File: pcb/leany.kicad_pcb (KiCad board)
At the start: 4 copper layers, 86.5 x 46.5 mm, 79 parts, among them J1 ST7735S, J2 SWD, J3 USB C, J4 2059-302/998-403, Q1 AO3401A, Q2 AO3400A, Q3 AO3401A, Q4 AO3401A, SW1 SW_HIGH, SW2 SW_HIGH, SW3 SW_LOW, SW4 POWER, U1 STM32F103C8Tx, U2 CH340N, U3 ICM-42688-P, U4 BQ25619, U5 AP6683, U7 AMS1117-3.3, Y1 8MHz

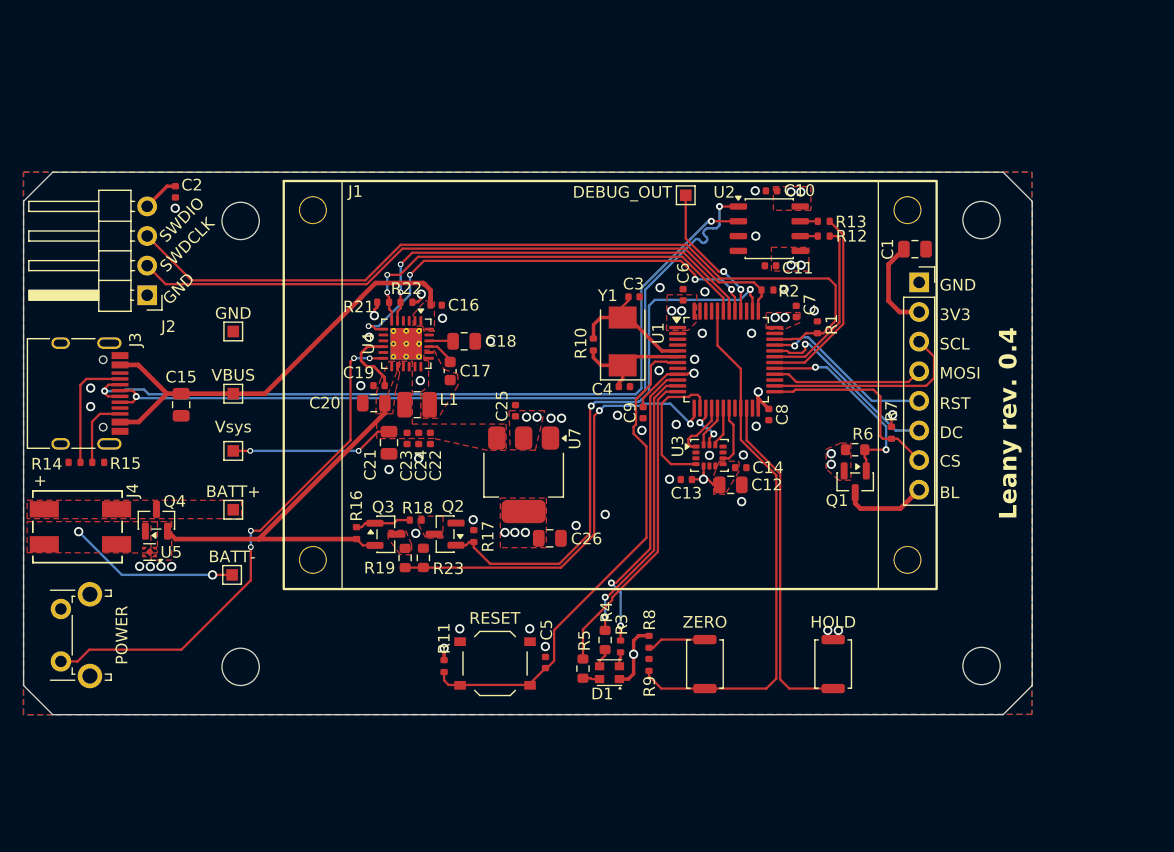
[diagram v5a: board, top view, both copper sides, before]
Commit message: refactor: fallback to rev 0.3 and update files (#98)
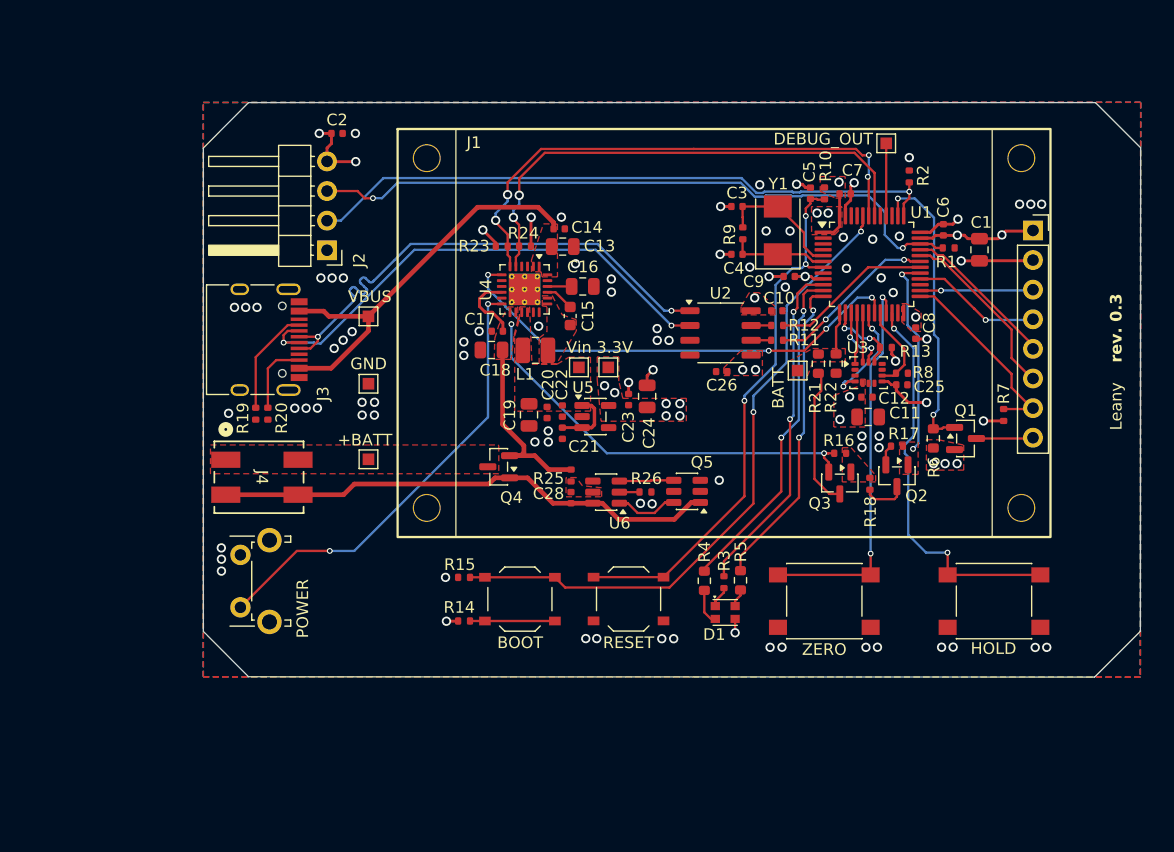
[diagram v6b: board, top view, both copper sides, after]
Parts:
- removed H1, H2, H3, H4: MountingHole, MountingHole:MountingHole_3.2mm_M3
- removed U7: AMS1117-3.3, Package_TO_SOT_SMD:SOT-223-3_TabPin2
- added C28: 100n, leany_footprints:C_0402_1005Metric, F.Cu at (136.5, 113.2)
- added Q5: PT8810, Package_TO_SOT_SMD:SOT-23-6, F.Cu at (146.5, 112.6)
- added R20: 5k1, leany_footprints:R_0402_1005Metric, F.Cu at (110.5, 106.0)
- added R24: 4k7, leany_footprints:R_0402_1005Metric, F.Cu at (132.6, 91.6)
- added R25: 100R, leany_footprints:R_0402_1005Metric, F.Cu at (136.5, 111.3)
- added R26: 1k, leany_footprints:R_0402_1005Metric, F.Cu at (142.9, 112.7)
- added SW5: POWER, Button_Switch_THT:SW_Tactile_SPST_Angled_PTS645Vx31-2LFS, F.Cu at (108.2, 122.6)
- added TP4: BATT, leany_footprints:TestPoint_Pad_1.0x1.0mm, F.Cu at (155.9, 102.3)
- added U6: DW01A, Package_TO_SOT_SMD:SOT-23-6, F.Cu at (139.5, 112.7)
- C11, C19: value 100n -> 10u; footprint leany_footprints:C_0402_1005Metric -> Capacitor_SMD:C_0805_2012Metric
- C12, C21, C26: value 10u -> 100n; footprint Capacitor_SMD:C_0805_2012Metric -> leany_footprints:C_0402_1005Metric
- C13: value 100n -> 22u; footprint leany_footprints:C_0402_1005Metric -> Capacitor_SMD:C_0805_2012Metric
- C14, C23: value 100n -> 1u
- C15: value 22u -> 47n; footprint Capacitor_SMD:C_0805_2012Metric -> Capacitor_SMD:C_0603_1608Metric
- C16: value 1u -> 4.7u; footprint leany_footprints:C_0402_1005Metric -> Capacitor_SMD:C_0805_2012Metric
- C17: value 47n -> 100n; footprint Capacitor_SMD:C_0603_1608Metric -> leany_footprints:C_0402_1005Metric
- C18: value 4.7u -> 10u
- C20: value 10u -> 22n; footprint Capacitor_SMD:C_0805_2012Metric -> leany_footprints:C_0402_1005Metric
- C22: value 22n -> 1u
- C24: value 1u -> 10u; footprint leany_footprints:C_0402_1005Metric -> Capacitor_SMD:C_0805_2012Metric
- C25: value 1u -> 100n
- D1: value NH-Z1921RGBA-SG -> NH-B2020RGBA-HF; footprint leany_footprints:NH-Z1921RGBA-SG -> leany_footprints:NH-B2020RGBA-HF
- J4: value 2059-302/998-403 -> BATT
- R10: value 1M -> 10k
- R11: value 10k -> 4k7
- R13: value 4k7 -> 10k
- R14: value 5k1 -> 10k
- R15: value 5k1 -> 100k
- R19: value 56k -> 5k1; footprint Resistor_SMD:R_0603_1608Metric -> leany_footprints:R_0402_1005Metric
- R21, R22: value 4k7 -> 56k; footprint leany_footprints:R_0402_1005Metric -> Resistor_SMD:R_0603_1608Metric
- R23: value 150k -> 4k7; footprint Resistor_SMD:R_0603_1608Metric -> leany_footprints:R_0402_1005Metric
- R8: value 10k -> 100k
- R9: value 100k -> 1M
- SW1: value SW_HIGH -> ZERO; footprint Button_Switch_SMD:SW_Push_SPST_NO_Alps_SKRK -> leany_footprints:SW_Push_1P1T_NO_6x6mm_H9.5mm
- SW2: value SW_HIGH -> HOLD; footprint Button_Switch_SMD:SW_Push_SPST_NO_Alps_SKRK -> leany_footprints:SW_Push_1P1T_NO_6x6mm_H9.5mm
- SW3: value SW_LOW -> RESET
- SW4: value POWER -> BOOT; footprint Button_Switch_THT:SW_Tactile_SPST_Angled_PTS645Vx31-2LFS -> leany_footprints:SW_Push_1P1T_XKB_TS-1187A
- TP5: value BATT+ -> +BATT
- TP6: value BATT- -> Vin
- TP7: value Vsys -> 3.3V
- U2: footprint Package_SO:JEITA_SOIC-8_3.9x4.9mm_P1.27mm -> leany_footprints:SOP-8_3.9x4.9mm_P1.27mm
- U5: value AP6683 -> AP2112K-3.3; footprint Package_DFN_QFN:UDFN-4-1EP_1x1mm_P0.65mm_EP0.48x0.48mm -> Package_TO_SOT_SMD:SOT-23-5
- moved C5 46.2 mm to (157.1, 87.0)
- moved R16 42.0 mm to (159.6, 109.4), turned to 180 degrees
- moved U5 40.0 mm to (138.6, 106.2), turned to 0 degrees
- moved R11 40.0 mm to (154.2, 99.7), turned to 180 degrees
- moved SW4 39.7 mm to (132.1, 121.9), turned to 180 degrees
- moved Q3 39.2 mm to (159.6, 111.9), turned to -90 degrees
- moved Q2 39.1 mm to (164.5, 111.3), turned to -90 degrees
- moved R18 39.1 mm to (162.2, 112.0), turned to -90 degrees
- moved R9 37.9 mm to (151.2, 90.5), turned to -90 degrees
- moved R21 37.7 mm to (157.7, 101.7), turned to -90 degrees
- moved R22 37.2 mm to (159.2, 101.7), turned to 90 degrees
- moved R17 37.1 mm to (164.5, 108.7), turned to 180 degrees
- moved R14 36.1 mm to (127.3, 123.7), turned to 0 degrees
- moved TP6 34.7 mm to (137.2, 102.0), turned to 0 degrees
- moved C15 34.2 mm to (136.4, 97.6), turned to 90 degrees
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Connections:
- net /DEBUG_SWCLK renamed /DEBUG_SWDCLK
- net /IMU_SCL renamed /IMU_SCK
- C13 pad 1: +3V3 -> Net-(U4-PSEL)
- C14 pad 1: +3V3 -> Net-(U4-PSEL)
- C15 pad 1: Net-(U4-PSEL) -> Net-(C15-Pad1)
- C15 pad 2: GND -> Net-(U4-BTST)
- C16 pad 1: Net-(U4-PSEL) -> Net-(U4-REGN)
- C17 pad 1: Net-(C17-Pad1) -> +BATT
- C17 pad 2: Net-(U4-BTST) -> GND
- C18 pad 1: Net-(U4-REGN) -> +BATT
- C19 pad 1: +BATT -> SYS
- C20 pad 1: +BATT -> SYS
- C21 pad 1: Net-(U7-VI) -> SYS
- C22 pad 1: Net-(U7-VI) -> SYS
- C23 pad 1: Net-(U7-VI) -> +3V3
- C24 pad 1: Net-(U7-VI) -> +3V3
- D1 pad 1: +3V3 -> Net-(D1-RK)
- D1 pad 2: Net-(D1-RK) -> Net-(D1-BK)
- D1 pad 3: Net-(D1-GK) -> +3V3
- D1 pad 4: Net-(D1-BK) -> Net-(D1-GK)
- J4 pad 3: PGND -> GNDREF
- J4 pad 4: PGND -> GNDREF
- L1 pad 1: Net-(C17-Pad1) -> Net-(C15-Pad1)
- L1 pad 2: Net-(U7-VI) -> SYS
- Q4 pad 1: PGND -> GNDREF
- R10 pad 1: Net-(U1-PD0) -> +3V3
- R10 pad 2: Net-(U1-PD1) -> Net-(U1-NRST)
- R11 pad 1: +3V3 -> /FTDI_RX
- R11 pad 2: Net-(U1-NRST) -> Net-(U2-TXD)
- R12 pad 1: /FTDI_RX -> /FTDI_TX
- R12 pad 2: Net-(U2-TXD) -> Net-(U2-RXD)
- R13 pad 1: /FTDI_TX -> +3V3
- R13 pad 2: Net-(U2-RXD) -> /IMU_CS
- R14 pad 1: Net-(J3-CC1) -> +3V3
- R14 pad 2: GND -> Net-(R14-Pad2)
- R15 pad 1: Net-(J3-CC2) -> /BOOT0
- R19 pad 1: BATT_VOLT -> Net-(J3-CC1)
- R19 pad 2: Net-(Q3-D) -> GND
- R21 pad 1: CHG_SDA -> BATT_VOLT
- R21 pad 2: +3V3 -> Net-(Q3-D)
- R22 pad 1: CHG_SCL -> GND
- R22 pad 2: +3V3 -> BATT_VOLT
- R23 pad 1: BATT_VOLT -> CHG_SDA
- R23 pad 2: GND -> +3V3
- R8 pad 1: +3V3 -> GND
- R8 pad 2: Net-(R8-Pad2) -> /IMU_INT2
- R9 pad 1: /ZERO_BUTTON -> Net-(U1-PD0)
- R9 pad 2: GND -> Net-(U1-PD1)
- SW1 pad 1: Net-(R8-Pad2) -> Net-(U1-PB10)
- SW1 pad 2: /ZERO_BUTTON -> GND
- SW4 pad 1: Net-(U4-~{QON}) -> Net-(R14-Pad2)
- SW4 pad 2: GND -> /BOOT0
- TP6 pad 1: PGND -> SYS
- TP7 pad 1: Net-(U7-VI) -> +3V3
- U1 pad 14: /IMU_INT1 -> /IMU_CS
- U1 pad 18: /IMU_CS -> /IMU_INT1
- U1 pad 19: /IMU_INT2 -> CHG_INT
- U1 pad 20: unconnected-(U1-PB2-Pad20) -> /IMU_INT2
- U1 pad 21: /ZERO_BUTTON -> Net-(U1-PB10)
- U1 pad 29: /ST7735S_BL -> BATT_EN
- U1 pad 38: BATT_EN -> /ST7735S_BL
- U1 pad 41: CHG_INT -> unconnected-(U1-PB5-Pad41)
- U1 pad 44: /ZERO_BUTTON -> /BOOT0
- U4 pad 15: Net-(U7-VI) -> SYS
- U4 pad 16: Net-(U7-VI) -> SYS
- U4 pad 19: Net-(C17-Pad1) -> Net-(C15-Pad1)
- U4 pad 20: Net-(C17-Pad1) -> Net-(C15-Pad1)
- U5 pad 1: +BATT -> SYS
- U5 pad 2: PGND -> GND
- U5 pad 3: PGND -> SYS
- U5 pad 4: GND -> unconnected-(U5-NC-Pad4)
- U5 pad 5: GND -> +3V3
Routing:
- net /BOOT0: track 0.00 -> 56.3 mm, vias 0 -> 2
- net /ZERO_BUTTON: track 45.8 -> 0.00 mm
- net GNDREF: track 0.00 -> 43.4 mm
- net BATT_VOLT: track 38.5 -> 3.66 mm, vias 2 -> 0
- net Net-(U1-PB10): track 0.00 -> 33.6 mm, vias 0 -> 2
- net BATT_EN: track 48.8 -> 17.4 mm
- net USB_D-: track 69.1 -> 44.4 mm
- net USB_D+: track 69.2 -> 44.7 mm
- net GND: track 0.00 -> 23.1 mm, vias 43 -> 80
- net +BATT: track 40.5 -> 58.5 mm, vias 0 -> 2
- net /DEBUG_SWDIO: track 72.3 -> 57.5 mm, vias 0 -> 2
- net PGND: track 14.7 -> 0.00 mm, vias 2 -> 0
- net Net-(U7-VI): track 14.1 -> 0.00 mm, vias 2 -> 0
- net Net-(Q3-D): track 0.00 -> 12.0 mm
- net CHG_SDA: track 36.2 -> 45.8 mm, vias 2 -> 4
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- added copper zone on F.Cu, net BATT_EN
- added copper zone on F.Cu, net BATT_VOLT
- added copper zone on F.Cu, net Net-(C15-Pad1)
- added copper zone on F.Cu, net Net-(Q3-G)
- added copper zone on F.Cu, net Net-(U6-VCC)
- added copper zone on F.Cu, net SYS
- removed copper zone on F.Cu, net Net-(C17-Pad1)
- removed copper zone on F.Cu, net Net-(Q2-D)
- removed copper zone on F.Cu, net Net-(Q3-D)
- removed copper zone on F.Cu, net Net-(U7-VI)
- removed copper zone on F.Cu, net PGND
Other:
- board size 86.5 x 46.5 mm -> 80.4 x 49.3 mm
- board text added: "0.2"
- board text added: "0.75"
- board text added: "18"
- board text added: "24"
- board text added: "7mm"
- board text added: "9mm"
- board text added: "Leany"
- board text added: "rev. 0.3"
- board text removed: "0.14"
- board text removed: "0.34"
- board text removed: "22"
- board text removed: "26"
- board text removed: "3V3"
- board text removed: "4mm"
- board text removed: "5.5mm"
- board text removed: "BL"
- board text removed: "CS"
- board text removed: "DC"
- board text removed: "GND"
- board text removed: "Leany rev. ${REVISION}"
- board text removed: "MOSI"
- board text removed: "RST"
- board text removed: "SCL"
- board text removed: "SWDCLK"
- board text removed: "SWDIO"
- board text removed: "TP6"

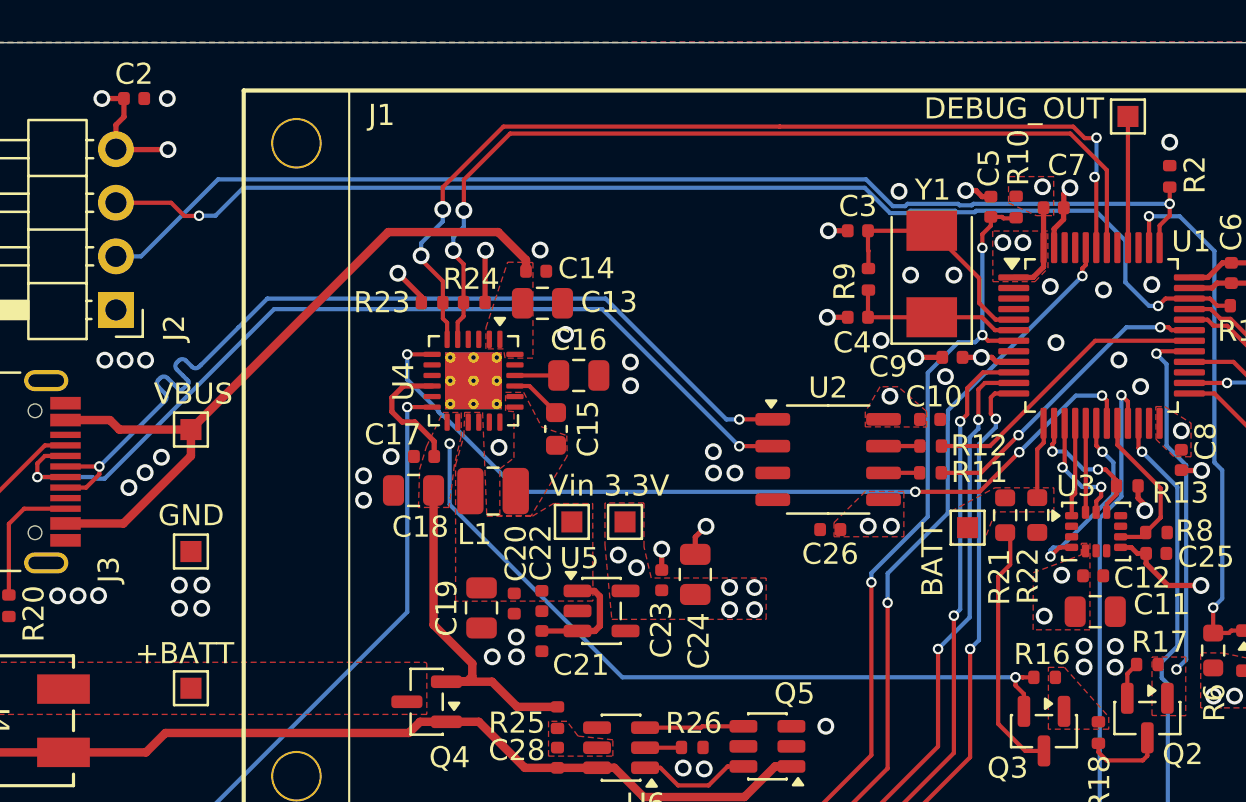
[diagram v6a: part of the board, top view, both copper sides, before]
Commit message: fix: remove test points from BOM  and CPL (#98)
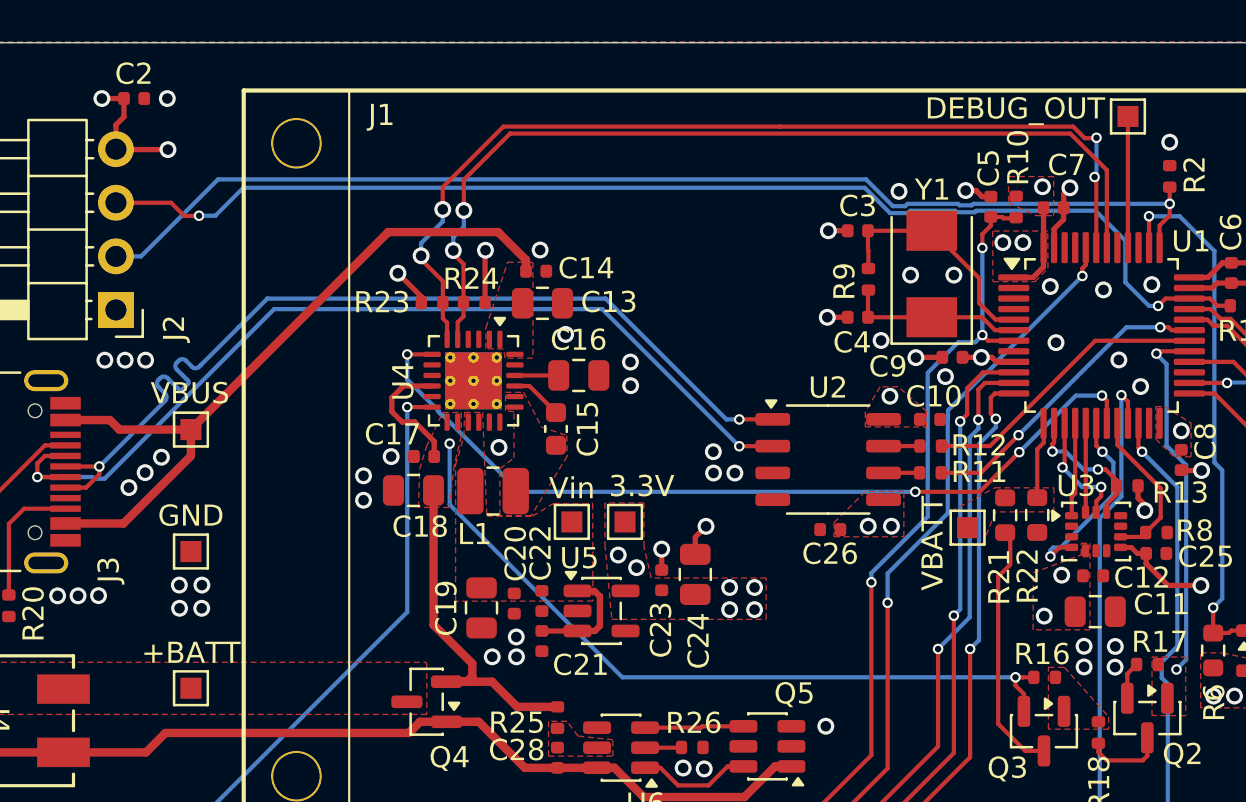
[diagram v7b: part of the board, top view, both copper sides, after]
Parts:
- TP4: value BATT -> VBATT
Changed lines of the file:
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@@
 		)
 		(property "Value" "3.3V"
-			(at 0.55 -1.71 0)
+			(at 0.7875 -1.685417 0)
 			(layer "F.SilkS")
 			(effects
@@
 			)
 		)
-		(property "LCSC" ""
-			(at 0 0 0)
-			(unlocked yes)
-			(layer "F.Fab")
-			(hide yes)
-			(effects
-				(font
-					(size 1 1)
-					(thickness 0.15)
-				)
-			)
-		)
 		(property ki_fp_filters "Pin* Test*")
 		(sheetname "/Power management/")
@@
 			)
 		)
-		(attr dnp)
+		(attr exclude_from_pos_files exclude_from_bom dnp)
 		(duplicate_pad_numbers_are_jumpers no)
 		(fp_line
@@
 		)
 		(fp_text user "${REFERENCE}"
-			(at 0.35 -1.71 0)
+			(at 0 0 0)
 			(layer "F.Fab")
 			(effects
@@
 		(tags "test point SMD pad rectangle square")
 		(property "Reference" "TP2"
-			(at 0 -1.71 0)
+			(at 0 -1.448 0)
 			(layer "F.Fab")
+			(hide yes)
 			(effects
 				(font
@@
 		)
 		(property "Value" "GND"
-			(at 0.01 -1.71 0)
+			(at 0 -1.69 0)
 			(layer "F.SilkS")
 			(effects
@@
 			)
 		)
-		(property "LCSC" ""
-			(at 0 0 0)
-			(unlocked yes)
-			(layer "F.Fab")
-			(hide yes)
-			(effects
-				(font
-					(size 1 1)
-					(thickness 0.15)
-				)
-			)
-		)
 		(property ki_fp_filters "Pin* Test*")
 		(sheetname "/Power management/")
@@
 			)
 		)
-		(attr dnp)
+		(attr exclude_from_pos_files exclude_from_bom dnp)
 		(duplicate_pad_numbers_are_jumpers no)
 		(fp_line
@@
 		)
 		(fp_text user "${REFERENCE}"
-			(at 0.01 0.04 0)
+			(at 0 0 0)
 			(layer "F.Fab")
 			(effects
@@
 		(tags "test point SMD pad rectangle square")
 		(property "Reference" "TP1"
-			(at 0 0.03 0)
+			(at 0 -1.448 0)
 			(layer "F.Fab")
+			(hide yes)
 			(effects
 				(font
@@
 		)
 		(property "Value" "DEBUG_OUT"
-			(at -5.4 -0.37 0)
+			(at -5.35 -0.37 0)
 			(layer "F.SilkS")
 			(effects
@@
 			)
 		)
-		(property "LCSC" ""
-			(at 0 0 0)
-			(unlocked yes)
-			(layer "F.Fab")
-			(hide yes)
-			(effects
-				(font
-					(size 1 1)
-					(thickness 0.15)
-				)
-			)
-		)
 		(property ki_fp_filters "Pin* Test*")
 		(sheetname "/")
@@
 			)
 		)
-		(attr dnp)
+		(attr exclude_from_pos_files exclude_from_bom dnp)
 		(duplicate_pad_numbers_are_jumpers no)
 		(fp_line
@@
 		)
 		(fp_text user "${REFERENCE}"
-			(at -2.4 -0.37 0)
+			(at 0 0 0)
 			(layer "F.Fab")
 			(effects
@@
 			)
 		)
-		(property "Value" "BATT"
-			(at 1.66 -1.5 270)
+		(property "Value" "VBATT"
+			(at 1.65 -0.74 270)
 			(layer "F.SilkS")
 			(effects
@@
 			)
 		)
-		(property "LCSC" ""
-			(at 0 0 180)
-			(unlocked yes)
-			(layer "F.Fab")
-			(hide yes)
-			(effects
-				(font
-					(size 1 1)
-					(thickness 0.15)
-				)
-			)
-		)
 		(property ki_fp_filters "Pin* Test*")
 		(sheetname "/Power management/")
@@
 			)
 		)
-		(attr dnp)
+		(attr exclude_from_pos_files exclude_from_bom dnp)
 		(duplicate_pad_numbers_are_jumpers no)
 		(fp_line
@@
 		)
 		(fp_text user "${REFERENCE}"
-			(at 1.65 -0.64 90)
+			(at 0 0 180)
 			(layer "F.Fab")
 			(effects
@@
 		)
 		(property "Value" "Vin"
-			(at 0 -1.71 0)
+			(at 0.0075 -1.585417 0)
 			(layer "F.SilkS")
 			(effects
@@
 			)
 		)
-		(property "LCSC" ""
-			(at 0 0 0)
-			(unlocked yes)
-			(layer "F.Fab")
-			(hide yes)
-			(effects
-				(font
-					(size 1 1)
-					(thickness 0.15)
-				)
-			)
-		)
 		(property ki_fp_filters "Pin* Test*")
 		(sheetname "/Power management/")
@@
 			)
 		)
-		(attr dnp)
+		(attr exclude_from_pos_files exclude_from_bom dnp)
 		(duplicate_pad_numbers_are_jumpers no)
 		(fp_line
@@
 		)
 		(fp_text user "${REFERENCE}"
-			(at 0 -1.71 0)
+			(at 0 0 0)
 			(layer "F.Fab")
 			(effects
@@
 		)
 		(property "Value" "+BATT"
-			(at -0.3 -1.65 0)
+			(at 0 -1.67 0)
 			(layer "F.SilkS")
 			(effects
@@
 			)
 		)
-		(property "LCSC" ""
-			(at 0 0 0)
-			(unlocked yes)
-			(layer "F.Fab")
-			(hide yes)
-			(effects
-				(font
-					(size 1 1)
-					(thickness 0.15)
-				)
-			)
-		)
 		(property ki_fp_filters "Pin* Test*")
 		(sheetname "/Power management/")
@@
 			)
 		)
-		(attr dnp)
+		(attr exclude_from_pos_files exclude_from_bom dnp)
 		(duplicate_pad_numbers_are_jumpers no)
 		(fp_line
@@
 		)
 		(fp_text user "${REFERENCE}"
-			(at 0 -1.67 0)
+			(at 0 0 0)
 			(layer "F.Fab")
 			(effects
@@
 		(tags "test point SMD pad rectangle square")
 		(property "Reference" "TP3"
-			(at 0 -1.69 0)
+			(at 0 -1.448 0)
 			(layer "F.Fab")
+			(hide yes)
 			(effects
 				(font
@@
 		)
 		(property "Value" "VBUS"
-			(at 0.11 -1.69 0)
+			(at -0.04 -1.71 0)
 			(layer "F.SilkS")
 			(effects
@@
 			)
 		)
-		(property "LCSC" ""
-			(at 0 0 0)
-			(unlocked yes)
-			(layer "F.Fab")
-			(hide yes)
-			(effects
-				(font
-					(size 1 1)
-					(thickness 0.15)
-				)
-			)
-		)
 		(property ki_fp_filters "Pin* Test*")
 		(sheetname "/Power management/")
@@
 			)
 		)
-		(attr dnp)
+		(attr exclude_from_pos_files exclude_from_bom dnp)
 		(duplicate_pad_numbers_are_jumpers no)
 		(fp_line
@@
 		)
 		(fp_text user "${REFERENCE}"
-			(at -0.09 0.11 0)
+			(at 0 0 0)
 			(layer "F.Fab")
 			(effects
